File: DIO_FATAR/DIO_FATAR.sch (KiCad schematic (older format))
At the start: 16 parts, among them J1 in, J2 thru, J3 right, J4 left, U1 74HC595, U2 74HC595, U3 74165, U4 74165

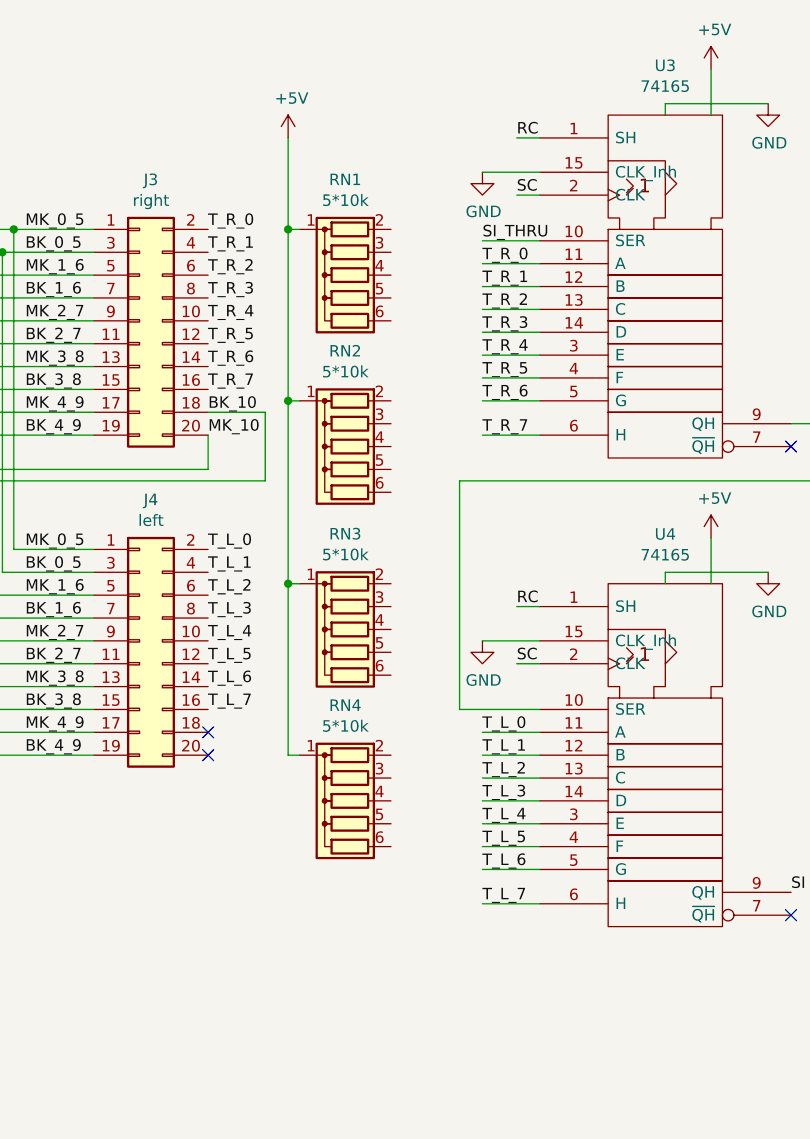
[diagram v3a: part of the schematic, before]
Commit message: DIO_FATAR: connect and roughly position resistor networks
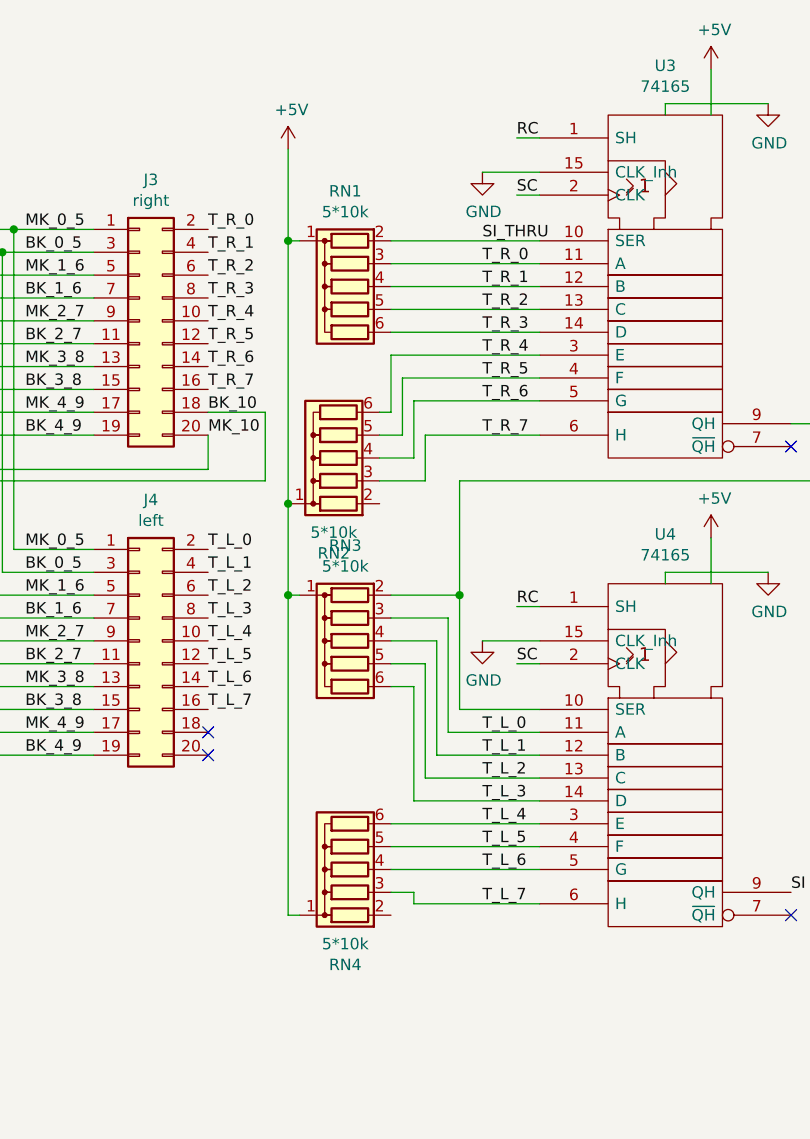
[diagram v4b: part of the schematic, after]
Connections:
- net SI_THRU: now also RN1.2 (R1)
- net T_L_0: now also RN3.3 (R2)
- net T_L_1: now also RN3.4 (R3)
- net T_L_2: now also RN3.5 (R4)
- net T_L_3: now also RN3.6 (R5)
- net T_L_4: now also RN4.6 (R5)
- net T_L_5: now also RN4.5 (R4)
- net T_L_6: now also RN4.4 (R3)
- net T_L_7: now also RN4.3 (R2)
- net T_R_0: now also RN1.3 (R2)
- net T_R_1: now also RN1.4 (R3)
- net T_R_2: now also RN1.5 (R4)
- net T_R_3: now also RN1.6 (R5)
- net T_R_4: now also RN2.6 (R5)
- net T_R_5: now also RN2.5 (R4)
- net T_R_6: now also RN2.4 (R3)
- net T_R_7: now also RN2.3 (R2)
- net at U3.9 (QH), U4.10 (SER): now also RN3.2 (R1)
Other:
- moved on the sheet: RN1, RN2, RN3, RN4
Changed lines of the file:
@@
 EESchema Schematic File Version 4
 LIBS:DIO_FATAR-cache
-EELAYER 26 0
+EELAYER 29 0
 EELAYER END
 $Descr A4 11693 8268
@@
 L Device:R_Network05 RN1
 U 1 1 5C64ADC8
-P 7150 1700
-F 0 "RN1" V 6733 1700 50  0000 C CNN
-F 1 "5*10k" V 6824 1700 50  0000 C CNN
-F 2 "Resistor_THT:R_Array_SIP6" V 7525 1700 50  0001 C CNN
-F 3 "http://www.vishay.com/docs/31509/csc.pdf" H 7150 1700 50  0001 C CNN
-	1    7150 1700
+P 7150 1750
+F 0 "RN1" V 6733 1750 50  0000 C CNN
+F 1 "5*10k" V 6824 1750 50  0000 C CNN
+F 2 "Resistor_THT:R_Array_SIP6" V 7525 1750 50  0001 C CNN
+F 3 "http://www.vishay.com/docs/31509/csc.pdf" H 7150 1750 50  0001 C CNN
+	1    7150 1750
 	0    -1   1    0
 $EndComp
@@
 Text Label 7750 3900 0    50   ~ 0
 T_L_2
-Wire Wire Line
-	8000 3700 7750 3700
-Wire Wire Line
-	8000 3800 7750 3800
-Wire Wire Line
-	7750 3900 8000 3900
-Wire Wire Line
-	8000 4000 7750 4000
-Wire Wire Line
-	7750 4100 8000 4100
-Wire Wire Line
-	8000 4200 7750 4200
-Wire Wire Line
-	7750 4300 8000 4300
-Wire Wire Line
-	7750 4450 8000 4450
 Text Notes 650  7500 0    50   ~ 0
 Left and Right are as seen from the playing position right before the keyboard
@@
 	8000 3600 7650 3600
 Wire Wire Line
-	7650 3600 7650 2600
+	7650 3600 7650 3100
 Wire Wire Line
 	7650 2600 9200 2600
@@
 Text Label 7750 1850 0    50   ~ 0
 T_R_2
-Wire Wire Line
-	8000 1650 7750 1650
-Wire Wire Line
-	8000 1750 7750 1750
-Wire Wire Line
-	7750 1850 8000 1850
-Wire Wire Line
-	8000 1950 7750 1950
-Wire Wire Line
-	7750 2050 8000 2050
-Wire Wire Line
-	8000 2150 7750 2150
-Wire Wire Line
-	7750 2250 8000 2250
-Wire Wire Line
-	7750 2400 8000 2400
 Text Label 7750 1550 0    50   ~ 0
 SI_THRU
-Wire Wire Line
-	7750 1550 8000 1550
 Text Label 7900 1350 0    50   ~ 0
 SC
@@
 L Device:R_Network05 RN2
 U 1 1 5C69FE8F
-P 7150 2450
-F 0 "RN2" V 6733 2450 50  0000 C CNN
-F 1 "5*10k" V 6824 2450 50  0000 C CNN
-F 2 "Resistor_THT:R_Array_SIP6" V 7525 2450 50  0001 C CNN
-F 3 "http://www.vishay.com/docs/31509/csc.pdf" H 7150 2450 50  0001 C CNN
-	1    7150 2450
-	0    -1   1    0
+P 7100 2500
+F 0 "RN2" V 6683 2500 50  0000 C CNN
+F 1 "5*10k" V 6774 2500 50  0000 C CNN
+F 2 "Resistor_THT:R_Array_SIP6" V 7475 2500 50  0001 C CNN
+F 3 "http://www.vishay.com/docs/31509/csc.pdf" H 7100 2500 50  0001 C CNN
+	1    7100 2500
+	0    -1   -1   0
 $EndComp
 $Comp
 L Device:R_Network05 RN3
 U 1 1 5C69FEE7
-P 7150 3250
-F 0 "RN3" V 6733 3250 50  0000 C CNN
-F 1 "5*10k" V 6824 3250 50  0000 C CNN
-F 2 "Resistor_THT:R_Array_SIP6" V 7525 3250 50  0001 C CNN
-F 3 "http://www.vishay.com/docs/31509/csc.pdf" H 7150 3250 50  0001 C CNN
-	1    7150 3250
+P 7150 3300
+F 0 "RN3" V 6733 3300 50  0000 C CNN
+F 1 "5*10k" V 6824 3300 50  0000 C CNN
+F 2 "Resistor_THT:R_Array_SIP6" V 7525 3300 50  0001 C CNN
+F 3 "http://www.vishay.com/docs/31509/csc.pdf" H 7150 3300 50  0001 C CNN
+	1    7150 3300
 	0    -1   1    0
 $EndComp
@@
 L Device:R_Network05 RN4
 U 1 1 5C69FF31
-P 7150 4000
-F 0 "RN4" V 6733 4000 50  0000 C CNN
-F 1 "5*10k" V 6824 4000 50  0000 C CNN
-F 2 "Resistor_THT:R_Array_SIP6" V 7525 4000 50  0001 C CNN
-F 3 "http://www.vishay.com/docs/31509/csc.pdf" H 7150 4000 50  0001 C CNN
-	1    7150 4000
-	0    -1   1    0
-$EndComp
-Wire Wire Line
-	6950 3800 6900 3800
-Wire Wire Line
-	6900 3800 6900 3050
-Wire Wire Line
-	6950 1500 6900 1500
-Connection ~ 6900 1500
-Wire Wire Line
-	6900 1500 6900 1100
-Wire Wire Line
-	6950 2250 6900 2250
-Connection ~ 6900 2250
-Wire Wire Line
-	6900 2250 6900 1500
-Wire Wire Line
-	6950 3050 6900 3050
-Connection ~ 6900 3050
-Wire Wire Line
-	6900 3050 6900 2250
+P 7150 4300
+F 0 "RN4" V 6733 4300 50  0000 C CNN
+F 1 "5*10k" V 6824 4300 50  0000 C CNN
+F 2 "Resistor_THT:R_Array_SIP6" V 7525 4300 50  0001 C CNN
+F 3 "http://www.vishay.com/docs/31509/csc.pdf" H 7150 4300 50  0001 C CNN
+	1    7150 4300
+	0    -1   -1   0
+$EndComp
+Wire Wire Line
+	6900 4500 6900 3100
+Wire Wire Line
+	6950 1550 6900 1550
+Connection ~ 6900 1550
+Wire Wire Line
+	6900 1550 6900 1150
+Wire Wire Line
+	6950 3100 6900 3100
+Connection ~ 6900 3100
+Wire Wire Line
+	6900 3100 6900 2700
 $Comp
 L power:+5V #PWR0107
 U 1 1 5C6AAD2A
-P 6900 1100
-F 0 "#PWR0107" H 6900 950 50  0001 C CNN
-F 1 "+5V" H 6915 1273 50  0000 C CNN
-F 2 "" H 6900 1100 50  0001 C CNN
-F 3 "" H 6900 1100 50  0001 C CNN
-	1    6900 1100
+P 6900 1150
+F 0 "#PWR0107" H 6900 1000 50  0001 C CNN
+F 1 "+5V" H 6915 1323 50  0000 C CNN
+F 2 "" H 6900 1150 50  0001 C CNN
+F 3 "" H 6900 1150 50  0001 C CNN
+	1    6900 1150
 	1    0    0    -1
 $EndComp
@@
 NoConn ~ 4450 3750
 NoConn ~ 4450 3850
+Wire Wire Line
+	7350 1550 8000 1550
+Wire Wire Line
+	7350 1650 8000 1650
+Wire Wire Line
+	7350 1750 8000 1750
+Wire Wire Line
+	7350 1850 8000 1850
+Wire Wire Line
+	7350 1950 8000 1950
+Wire Wire Line
+	7350 2050 7350 2300
+Wire Wire Line
+	7350 2050 8000 2050
+Wire Wire Line
+	7400 2150 7400 2400
+Wire Wire Line
+	7400 2150 8000 2150
+Wire Wire Line
+	7450 2250 7450 2500
+Wire Wire Line
+	7450 2250 8000 2250
+Wire Wire Line
+	7500 2400 7500 2600
+Wire Wire Line
+	7500 2400 8000 2400
+Wire Wire Line
+	7350 3100 7650 3100
+Connection ~ 7650 3100
+Wire Wire Line
+	7650 3100 7650 2600
+Wire Wire Line
+	7600 3700 7600 3200
+Wire Wire Line
+	7600 3200 7350 3200
+Wire Wire Line
+	7600 3700 8000 3700
+Wire Wire Line
+	7550 3800 7550 3300
+Wire Wire Line
+	7550 3300 7350 3300
+Wire Wire Line
+	7550 3800 8000 3800
+Wire Wire Line
+	7500 3900 7500 3400
+Wire Wire Line
+	7500 3400 7350 3400
+Wire Wire Line
+	7500 3900 8000 3900
+Wire Wire Line
+	7450 4000 7450 3500
+Wire Wire Line
+	7450 3500 7350 3500
+Wire Wire Line
+	7450 4000 8000 4000
+Wire Wire Line
+	7350 4100 8000 4100
+Wire Wire Line
+	7350 4200 8000 4200
+Wire Wire Line
+	7350 4300 8000 4300
+Wire Wire Line
+	7450 4450 7450 4400
+Wire Wire Line
+	7450 4400 7350 4400
+Wire Wire Line
+	7450 4450 8000 4450
+Wire Wire Line
+	7350 2300 7300 2300
+Wire Wire Line
+	7300 2400 7400 2400
+Wire Wire Line
+	7300 2500 7450 2500
+Wire Wire Line
+	7300 2600 7500 2600
+Connection ~ 6900 2700
+Wire Wire Line
+	6900 1550 6900 2700
+Wire Wire Line
+	6900 4500 6950 4500
 $EndSCHEMATC

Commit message: DIO_FATAR: route everything except two resistors
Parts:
- added R? (x2): 10k, symbol Device:R
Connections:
- net +5V: now also U2.16 (VCC), R?.1, R?.1
- net SI_THRU: now also R?.2; no longer RN1.2 (R1)
- net at U3.9 (QH), U4.10 (SER): now also R?.2; no longer RN3.2 (R1)
- net at U1.9 (QH'), U2.14 (SER): no longer U2.16 (VCC)
- no-connect marks 10 -> 14
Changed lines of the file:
@@
-$EndComp
-$Comp
-L Device:R_Network05 RN1
-U 1 1 5C64ADC8
-P 7150 1750
-F 0 "RN1" V 6733 1750 50  0000 C CNN
-F 1 "5*10k" V 6824 1750 50  0000 C CNN
-F 2 "Resistor_THT:R_Array_SIP6" V 7525 1750 50  0001 C CNN
-F 3 "http://www.vishay.com/docs/31509/csc.pdf" H 7150 1750 50  0001 C CNN
-	1    7150 1750
-	0    -1   1    0
 $EndComp
 $Comp
@@
 	8000 3600 7650 3600
 Wire Wire Line
-	7650 3600 7650 3100
-Wire Wire Line
 	7650 2600 9200 2600
 Wire Wire Line
@@
 $EndComp
 Wire Wire Line
-	3200 3550 3650 3550
+	3200 3550 3450 3550
 Text Label 3550 2200 0    50   ~ 0
 SO
@@
 	3450 1900 3650 1900
 Wire Wire Line
-	3450 3850 3450 4050
-Wire Wire Line
 	3450 4050 4050 4050
-Connection ~ 3450 3850
-Wire Wire Line
-	3450 3850 3650 3850
 Text Label 4450 2950 0    50   ~ 0
 SO_THRU
-Wire Wire Line
-	2950 3850 3450 3850
 $Comp
 L power:GND #PWR0112
@@
 NoConn ~ 4450 3850
 Wire Wire Line
-	7350 1550 8000 1550
-Wire Wire Line
 	7350 1650 8000 1650
 Wire Wire Line
@@
 Wire Wire Line
 	7500 2400 8000 2400
-Wire Wire Line
-	7350 3100 7650 3100
-Connection ~ 7650 3100
-Wire Wire Line
-	7650 3100 7650 2600
 Wire Wire Line
 	7600 3700 7600 3200
@@
 Wire Wire Line
 	6900 4500 6950 4500
+Wire Wire Line
+	2950 3850 3650 3850
+Wire Wire Line
+	3450 4050 3450 3550
+Connection ~ 3450 3550
+Wire Wire Line
+	3450 3550 3650 3550
+Wire Wire Line
+	7650 2600 7650 3600
+$Comp
+L Device:R R?
+U 1 1 5D186C46
+P 7450 1400
+F 0 "R?" H 7520 1446 50  0000 L CNN
+F 1 "10k" H 7520 1355 50  0000 L CNN
+F 2 "" V 7380 1400 50  0001 C CNN
+F 3 "~" H 7450 1400 50  0001 C CNN
+	1    7450 1400
+	1    0    0    -1
+$EndComp
+$Comp
+L Device:R R?
+U 1 1 5D187152
+P 9200 2200
+F 0 "R?" H 9270 2246 50  0000 L CNN
+F 1 "10k" H 9270 2155 50  0000 L CNN
+F 2 "" V 9130 2200 50  0001 C CNN
+F 3 "~" H 9200 2200 50  0001 C CNN
+	1    9200 2200
+	1    0    0    -1
+$EndComp
+Connection ~ 9200 2350
+Wire Wire Line
+	7450 1550 8000 1550
+$Comp
+L Device:R_Network05 RN1
+U 1 1 5C64ADC8
+P 7150 1750
+F 0 "RN1" V 6733 1750 50  0000 C CNN
+F 1 "5*10k" V 6824 1750 50  0000 C CNN
+F 2 "Resistor_THT:R_Array_SIP6" V 7525 1750 50  0001 C CNN
+F 3 "http://www.vishay.com/docs/31509/csc.pdf" H 7150 1750 50  0001 C CNN
+	1    7150 1750
+	0    -1   1    0
+$EndComp
+NoConn ~ 7350 1550
+NoConn ~ 7300 2700
+NoConn ~ 7350 3100
+NoConn ~ 7350 4500
+$Comp
+L power:+5V #PWR?
+U 1 1 5D1B93A5
+P 7450 1250
+F 0 "#PWR?" H 7450 1100 50  0001 C CNN
+F 1 "+5V" H 7465 1423 50  0000 C CNN
+F 2 "" H 7450 1250 50  0001 C CNN
+F 3 "" H 7450 1250 50  0001 C CNN
+	1    7450 1250
+	1    0    0    -1
+$EndComp
+$Comp
+L power:+5V #PWR?
+U 1 1 5D1B9642
+P 9200 2050
+F 0 "#PWR?" H 9200 1900 50  0001 C CNN
+F 1 "+5V" H 9215 2223 50  0000 C CNN
+F 2 "" H 9200 2050 50  0001 C CNN
+F 3 "" H 9200 2050 50  0001 C CNN
+	1    9200 2050
+	1    0    0    -1
+$EndComp
 $EndSCHEMATC
